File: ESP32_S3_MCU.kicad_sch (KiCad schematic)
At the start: 43 parts, among them SW1 SW_Push, SW2 SW_Push, SW3 SW_Push, SW4 SW_Push, U4 ESP32-S3-WROOM-1, U6 W25Q32JVSS, U8 ESP32-S3, X2 40MHz, X3 32.768KHz

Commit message: Replace MCU with WROOM-1 unit + route
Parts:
- removed C20, C24, C29, C30, C31, C32, C54, C57: 100n, Capacitor_SMD:C_0402_1005Metric, symbol Device:C_Small
- removed C21, C22: 3p3, Capacitor_SMD:C_0402_1005Metric, symbol Device:C_Small
- removed C23, C26: 20p, Capacitor_SMD:C_0402_1005Metric, symbol Device:C_Small
- removed C25, C28, C53: 1u, Capacitor_SMD:C_0402_1005Metric, symbol Device:C_Small
- removed C27: 10u, Capacitor_SMD:C_0603_1608Metric, symbol Device:C_Small
- removed C33: 10nF, Capacitor_SMD:C_0402_1005Metric, symbol Device:C_Small
- removed C34: 1uF, Capacitor_SMD:C_0402_1005Metric, symbol Device:C_Small
- removed L2, L3: 2n2, Inductor_SMD:L_0402_1005Metric, symbol Device:L_Small
- removed R21: 10k, symbol Device:R_Small
- removed R22, R23: 5k1, Resistor_SMD:R_0603_1608Metric, symbol Device:R_Small
- removed SW1, SW3: SW_Push, Button_Switch_SMD:SW_Push_SPST_NO_Alps_SKRK, symbol Switch:SW_Push
- removed U6: W25Q32JVSS, Package_SO:SOIC-8_5.23x5.23mm_P1.27mm, symbol Memory_Flash:W25Q32JVSS
- removed U7: ~, RF_Antenna:Texas_SWRA117D_2.4GHz_Left, symbol Device:Small_Size_PCB_Antenna_2.4GHz
- removed U8: ESP32-S3, Package_DFN_QFN:QFN-56-1EP_7x7mm_P0.4mm_EP5.6x5.6mm, symbol PCM_Espressif:ESP32-S3
- removed X2: 40MHz, KiCADv7:OSC_X322516MLB4SI, symbol Device:Crystal_GND24_Small
- C19: value 10u -> 100n; footprint Capacitor_SMD:C_0603_1608Metric -> Capacitor_SMD:C_0402_1005Metric
- C9: value 100n -> 22u
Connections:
- net CHIP_BOOT is gone; now on net BOOT: C16.1, R10.2, SW4.2
- net RXD0 is gone; now on net GPIO44_RX: U4.36 (RXD0)
- net SPID is gone; now on net +3V3: R12.1
- net TXD0 is gone; now on net GPIO43_TX: U4.37 (TXD0)
- net VDD_SPI is gone; now on net ENABLE: C19.1
- net +3V3: no longer R12.2, R8.1
- net ENABLE: now also R12.2, R8.1
- net INT_IMU: now also U4.6 (IO6)
- net SCL: now also U4.5 (IO5)
- net SDA: now also U4.4 (IO4)
- net RESET: no longer names the net of C15.1, R8.2, SW2.2
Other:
- note removed: "RF ANTENNA"
- note removed: "SPI Flash Memory"
- note removed: "Za = 50R"
- note removed: "Zc = 35 + 10j"
- moved on the sheet: C10, C55, C56, C9, U4, X3

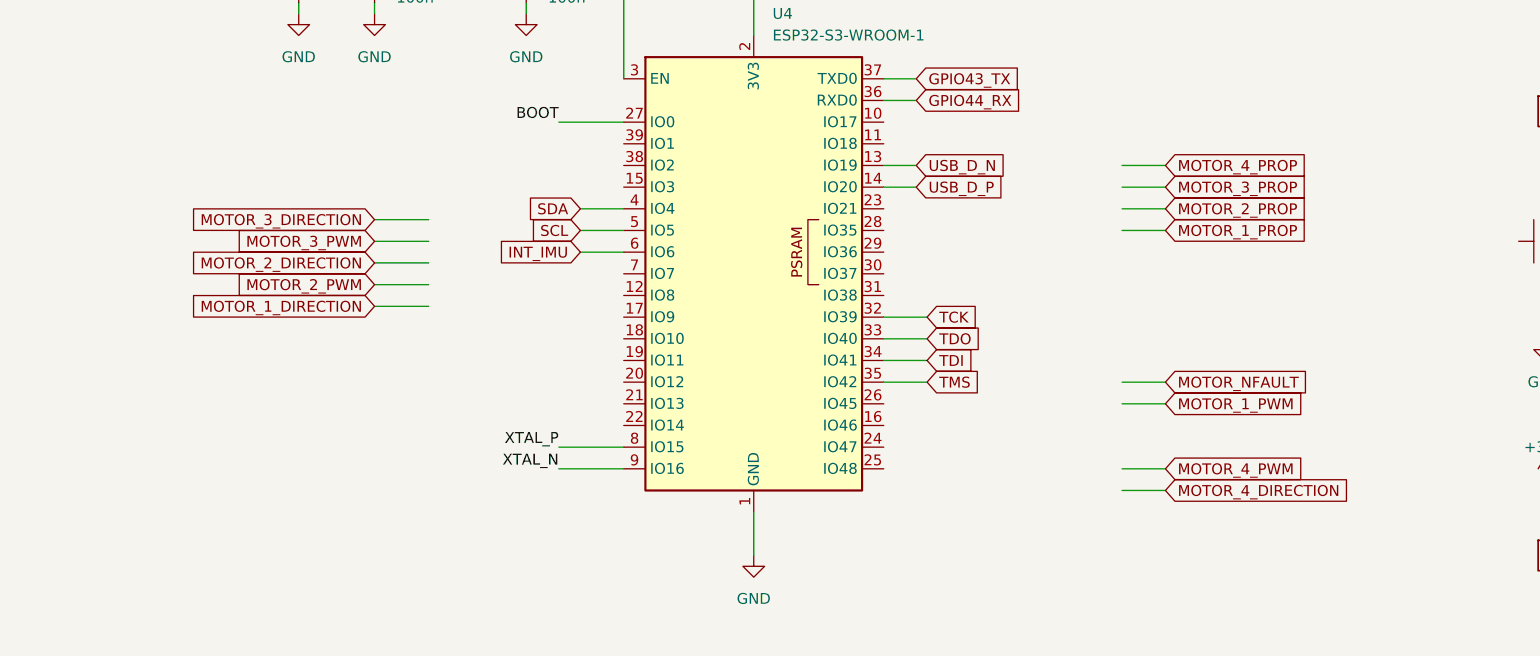
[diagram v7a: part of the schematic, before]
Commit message: Route Motor Drivers
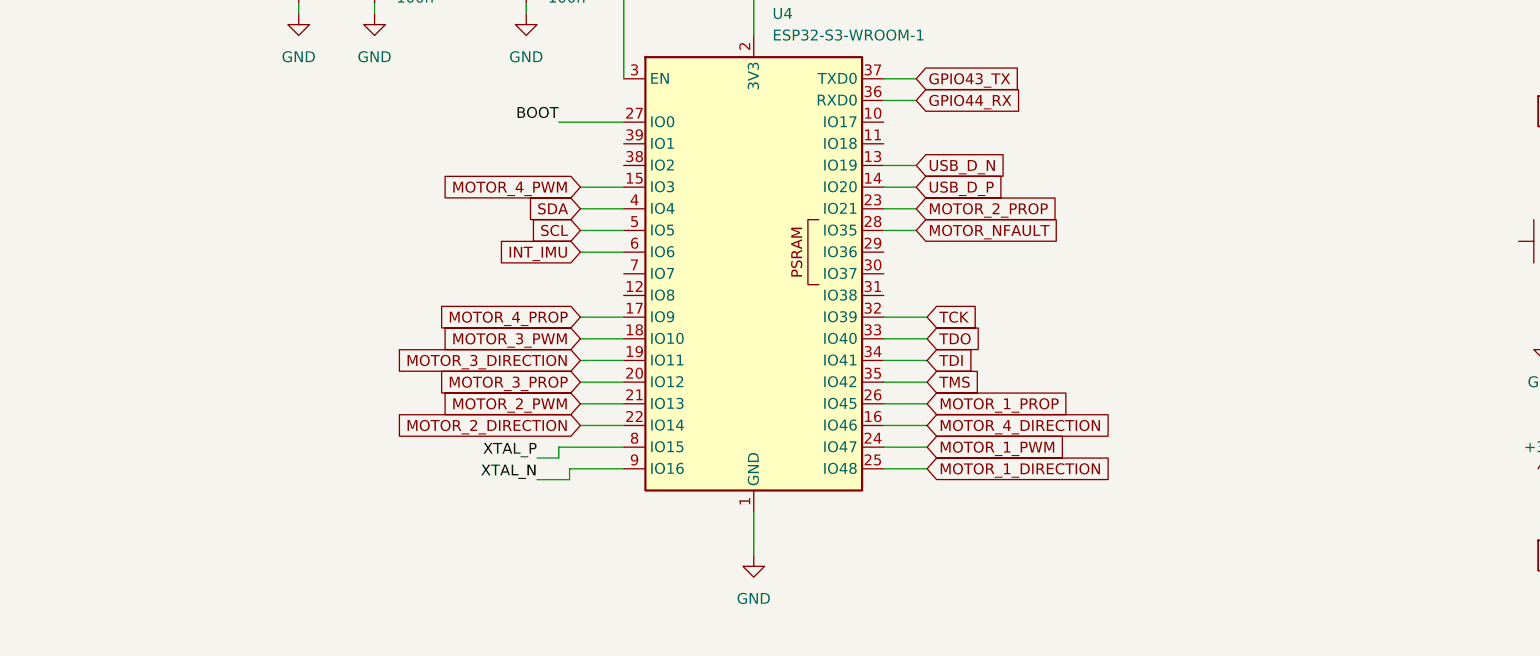
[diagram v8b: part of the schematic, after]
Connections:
- net MOTOR_1_DIRECTION: now also U4.25 (IO48)
- net MOTOR_1_PROP: now also U4.26 (IO45)
- net MOTOR_1_PWM: now also U4.24 (IO47)
- net MOTOR_2_DIRECTION: now also U4.22 (IO14)
- net MOTOR_2_PROP: now also U4.23 (IO21)
- net MOTOR_2_PWM: now also U4.21 (IO13)
- net MOTOR_3_DIRECTION: now also U4.19 (IO11)
- net MOTOR_3_PROP: now also U4.20 (IO12)
- net MOTOR_3_PWM: now also U4.18 (IO10)
- net MOTOR_4_DIRECTION: now also U4.16 (IO46)
- net MOTOR_4_PROP: now also U4.17 (IO9)
- net MOTOR_4_PWM: now also U4.15 (IO3)
- net MOTOR_NFAULT: now also U4.28 (IO35)
